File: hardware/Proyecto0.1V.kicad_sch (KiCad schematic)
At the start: 5 parts, among them J1 Conn_01x04, J2 Conn_01x04

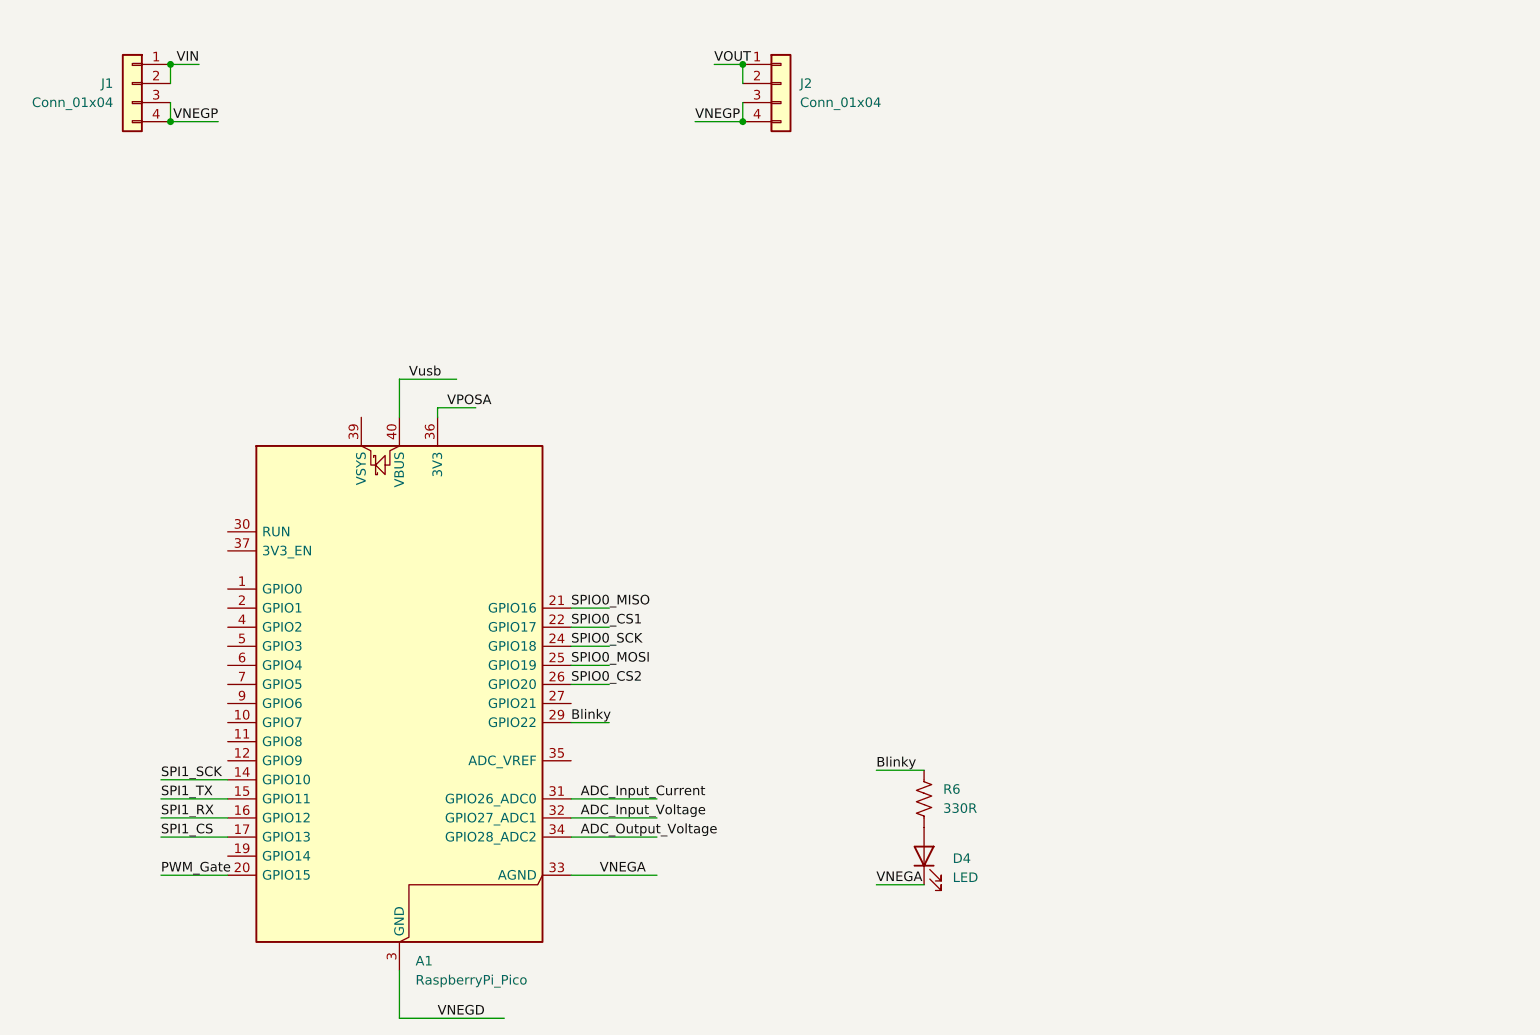
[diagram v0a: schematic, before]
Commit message: HW: Footprints, Descriptions and LCSC part number added to sch
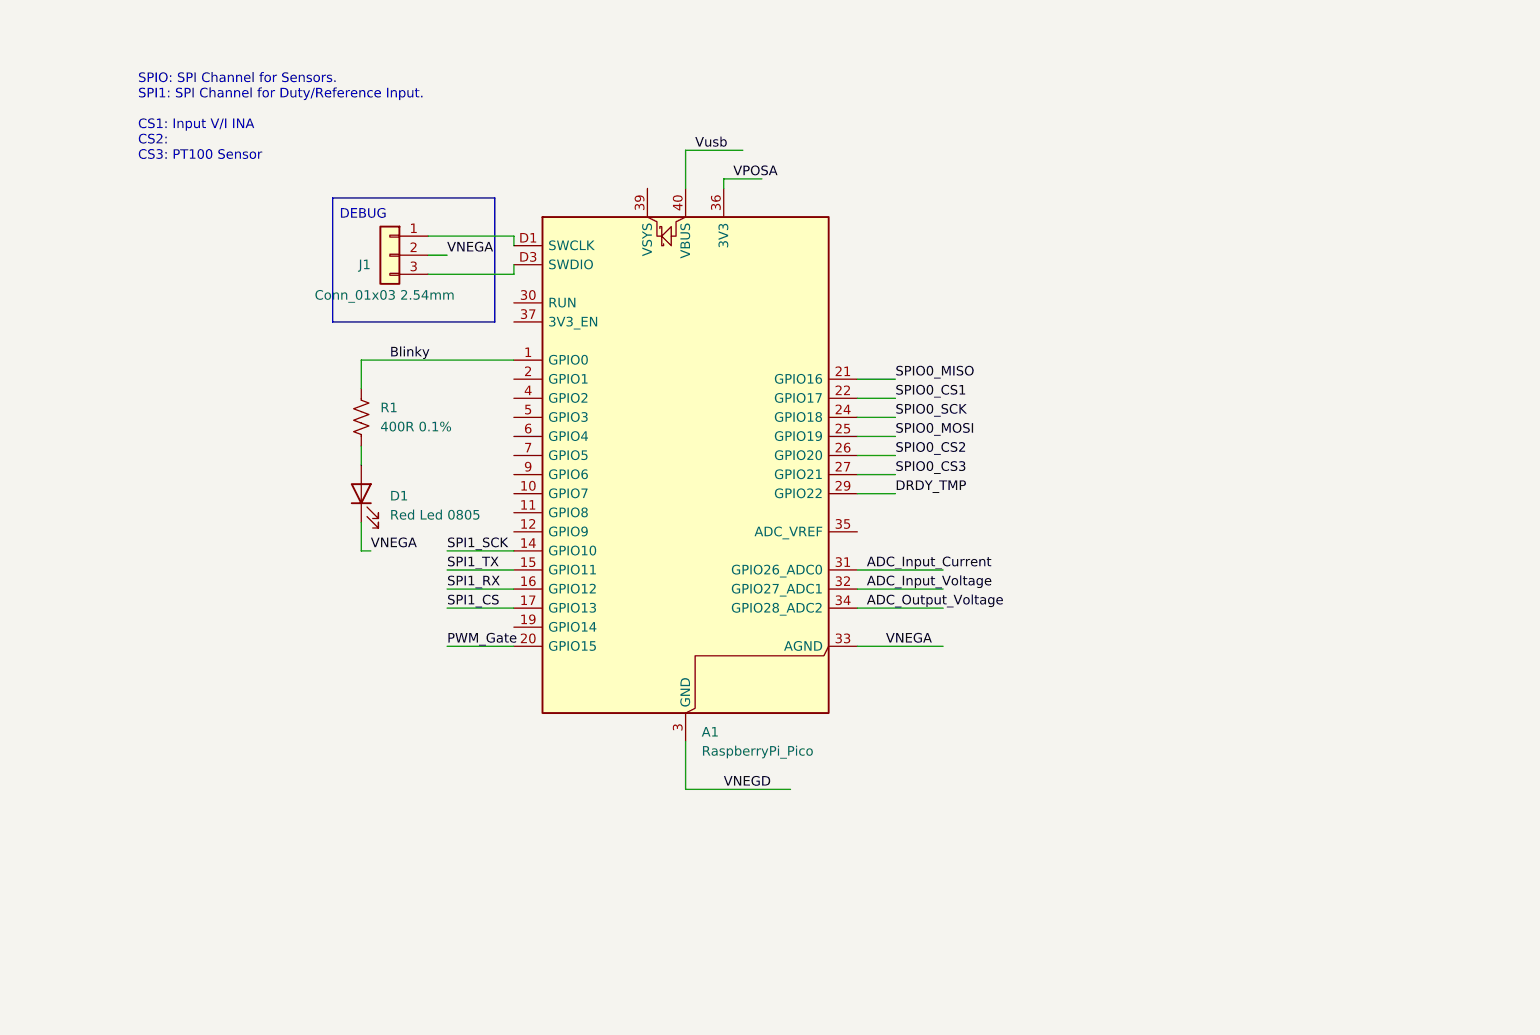
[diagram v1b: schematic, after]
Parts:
- removed A1: RaspberryPi_Pico, Module:RaspberryPi_Pico_Common_Unspecified, symbol MCU_Module:RaspberryPi_Pico
- removed J1, J2: Conn_01x04, symbol Connector_Generic:Conn_01x04
- added A1: RaspberryPi_Pico, Module:RaspberryPi_Pico_SMD_HandSolder, symbol MCU_Module:RaspberryPi_Pico_Debug
- added J1: Conn_01x03 2.54mm, Connector_PinHeader_2.54mm:PinHeader_1x03_P2.54mm_Vertical, symbol Connector_Generic:Conn_01x03
- D1: renamed from D4; value LED -> Red Led 0805; footprint (none) -> LED_SMD:LED_0805_2012Metric_Pad1.15x1.40mm_HandSolder; LCSC Part (none) -> C19171391
- R1: renamed from R6; value 330R -> 400R 0.1%; footprint (none) -> Resistor_SMD:R_0805_2012Metric_Pad1.20x1.40mm_HandSolder; LCSC Part (none) -> C153298
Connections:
- net ADC_Input_Current: now also A1.31 (GPIO26_ADC0)
- net ADC_Input_Voltage: now also A1.32 (GPIO27_ADC1)
- net ADC_Output_Voltage: now also A1.34 (GPIO28_ADC2)
- net Blinky: now also A1.1 (GPIO0)
- net PWM_Gate: now also A1.20 (GPIO15)
- net SPI1_CS: now also A1.17 (GPIO13)
- net SPI1_RX: now also A1.16 (GPIO12)
- net SPI1_SCK: now also A1.14 (GPIO10)
- net SPI1_TX: now also A1.15 (GPIO11)
- net SPIO0_CS1: now also A1.22 (GPIO17)
- net SPIO0_CS2: now also A1.26 (GPIO20)
- net SPIO0_MISO: now also A1.21 (GPIO16)
- net SPIO0_MOSI: now also A1.25 (GPIO19)
- net SPIO0_SCK: now also A1.24 (GPIO18)
- net VNEGA: now also A1.33 (AGND), J1.2 (Pin_2)
- net VNEGD: now also A1.13 (GND), A1.18 (GND), A1.23 (GND), A1.28 (GND), A1.3 (GND), A1.38 (GND), A1.8 (GND), A1.D2 (GND)
- net VPOSA: now also A1.36 (3V3)
- net Vusb: now also A1.40 (VBUS)
- new net: A1.D1 (SWCLK), J1.1 (Pin_1)
- new net: A1.D3 (SWDIO), J1.3 (Pin_3)
- new net DRDY_TMP: A1.29 (GPIO22)
- new net SPIO0_CS3: A1.27 (GPIO21)
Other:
- note added: "DEBUG"
- note added: "SPIO: SPI Channel for Sensors. SPI1: SPI Channel for Duty/Reference Input. CS1: Input V/I INA CS2: CS3: PT100 Sensor"
- moved on the sheet: D1, R1

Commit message: HW: sch near final version
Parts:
- removed A1: RaspberryPi_Pico, Module:RaspberryPi_Pico_SMD_HandSolder, symbol MCU_Module:RaspberryPi_Pico_Debug
- removed D1: Red Led 0805, LED_SMD:LED_0805_2012Metric_Pad1.15x1.40mm_HandSolder, symbol Device:LED
- removed J1: Conn_01x03 2.54mm, Connector_PinHeader_2.54mm:PinHeader_1x03_P2.54mm_Vertical, symbol Connector_Generic:Conn_01x03
- removed R1: 400R 0.1%, Resistor_SMD:R_0805_2012Metric_Pad1.20x1.40mm_HandSolder, symbol Device:R_US
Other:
- added sheet AnalogConverters (untitled.kicad_sch)
- added sheet Pico (Pico.kicad_sch)
- added sheet SepicConverter (SepicConverter.kicad_sch)
- added sheet Supplies (supplies.kicad_sch)
- note removed: "DEBUG"
- note removed: "SPIO: SPI Channel for Sensors. SPI1: SPI Channel for Duty/Reference Input. CS1: Input V/I INA CS2: CS3: PT100 Sensor"

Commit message: HW: Sch done. PCB WIP
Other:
- sheet Supplies ports: added GNDPWR; removed VDC
